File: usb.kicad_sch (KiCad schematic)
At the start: 53 parts, among them Q1 PJE138K, U1 MPFS250T-FCVG484, U13 USB3315-CP-TR, U15 SN74LVC1G04_SOT, U22 PI3USB102GZLEX, U23 PI3USB102GZLEX, U28 USB2422-I/MJ, Y1 Oscillator_24MHz_ESC_2016MV

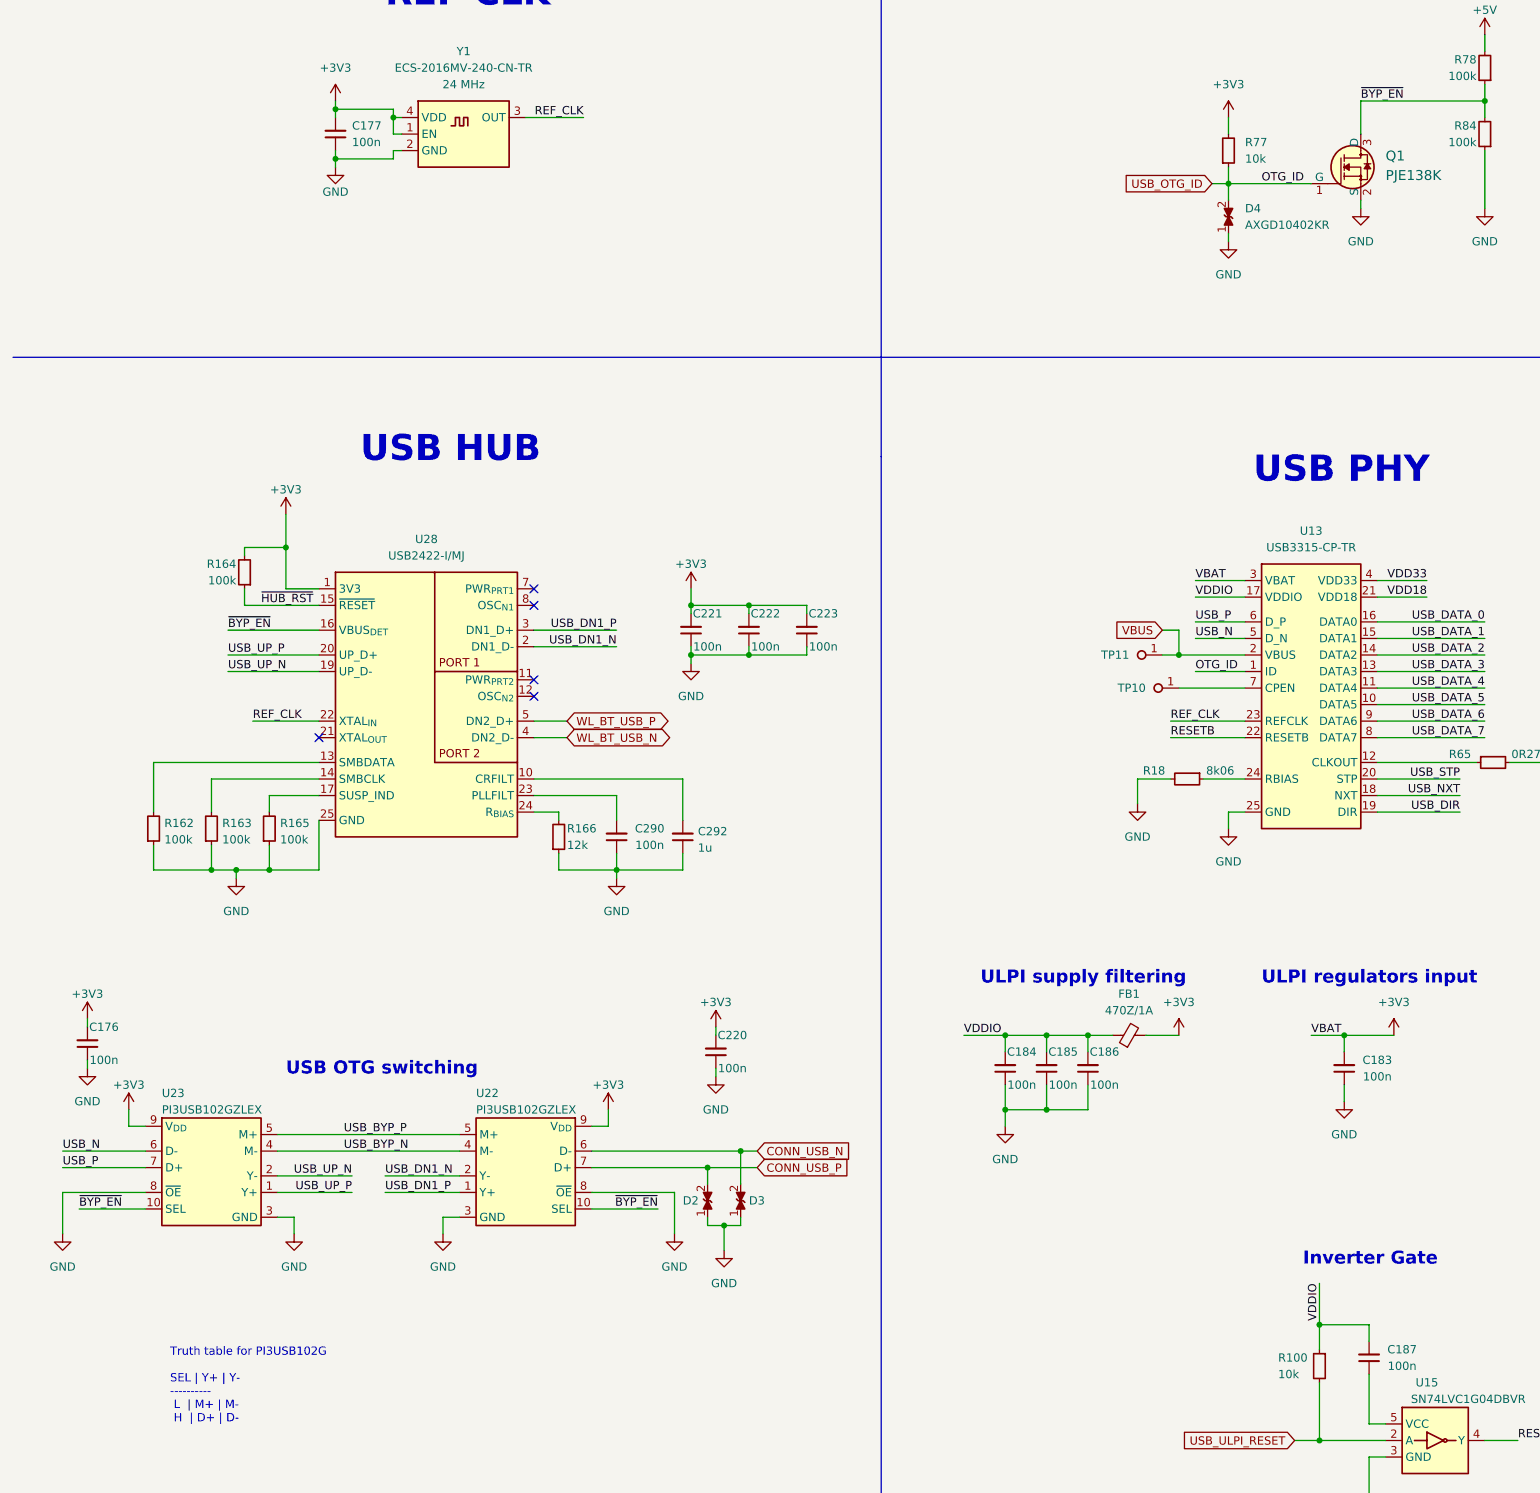
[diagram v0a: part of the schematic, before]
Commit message: [#56156] Create USB layout
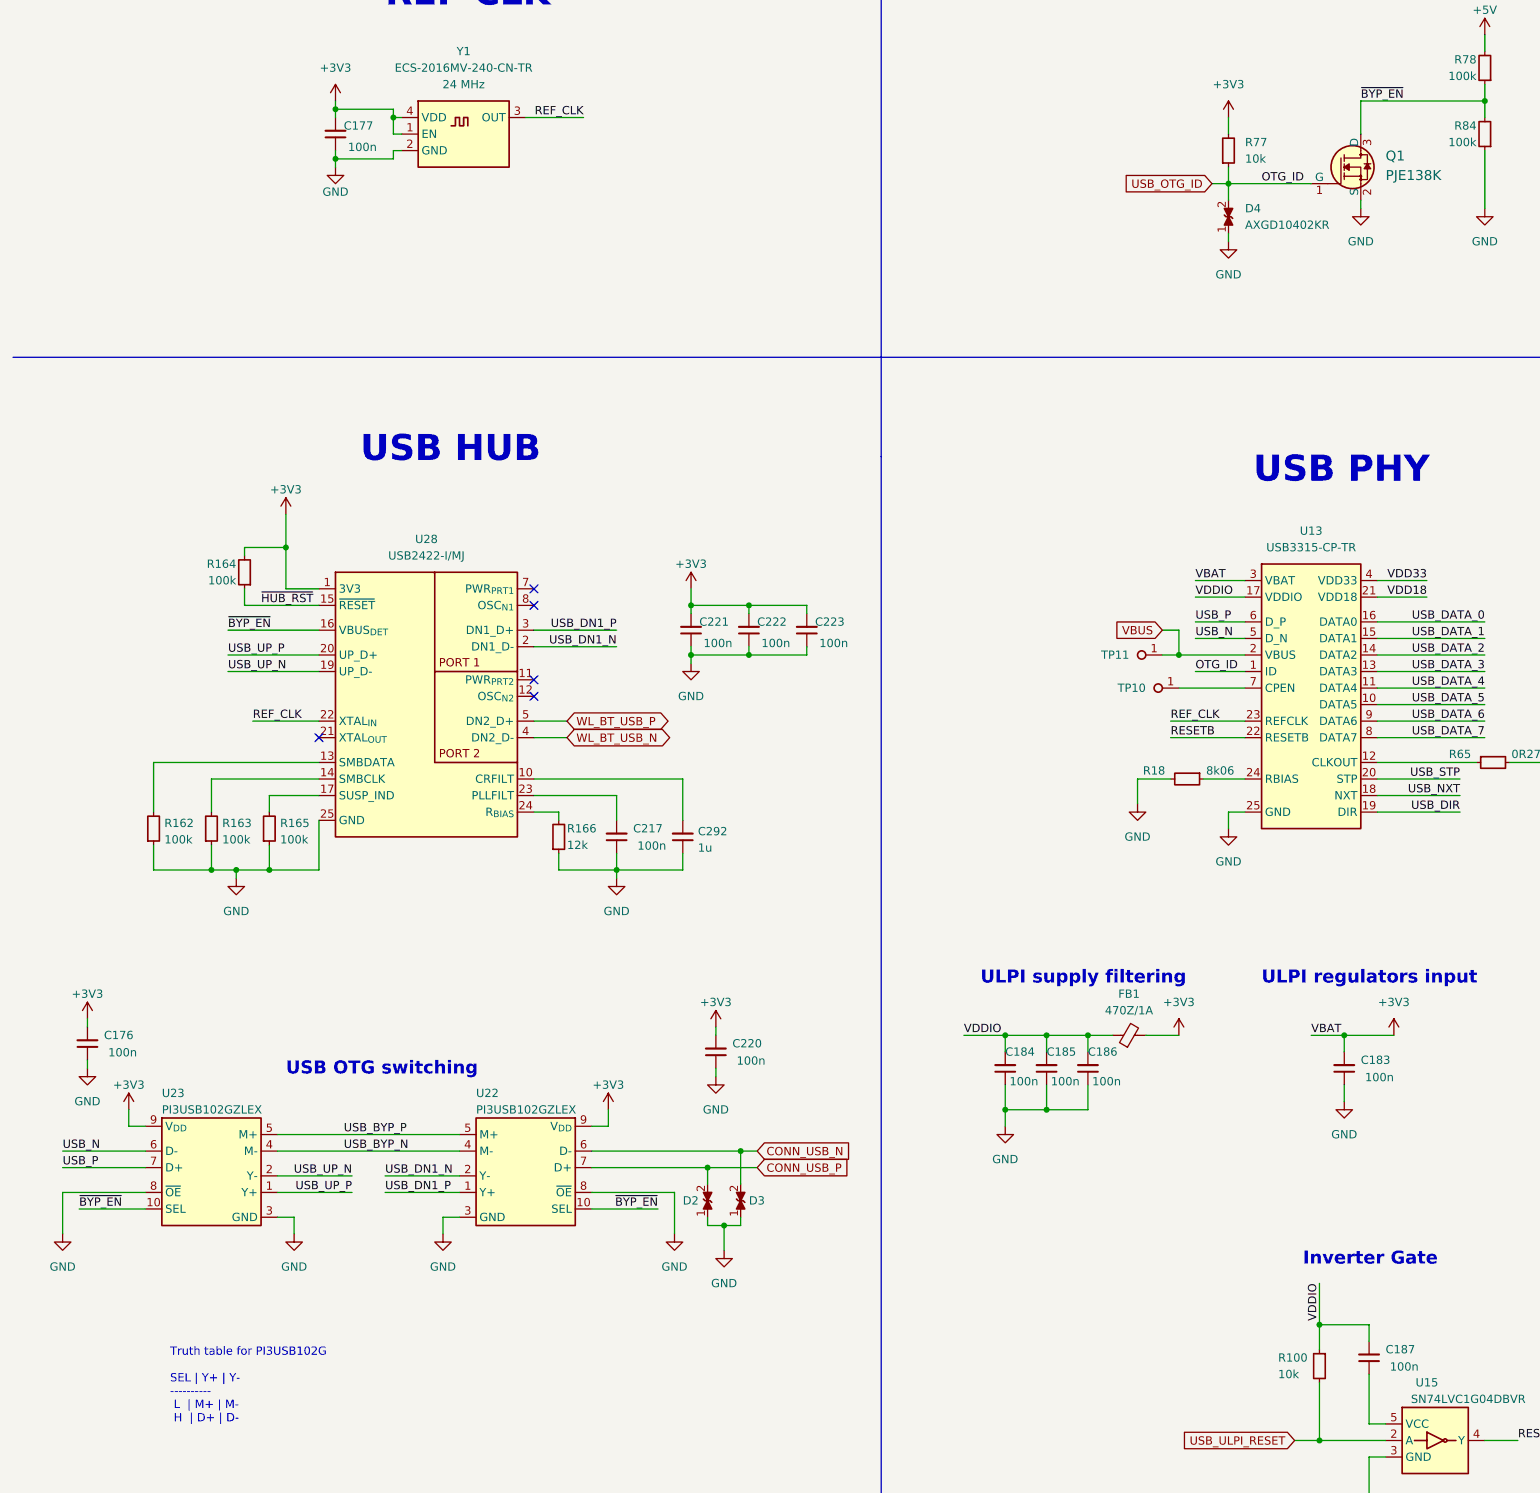
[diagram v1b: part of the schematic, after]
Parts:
- removed C176, C177, C183, C184, C185, C186, C187, C220, C221, C222, C223, C290: C_100n_0201_25V, antmicro-footprints:C_0201, symbol antmicroCapacitorsmisc:C_100n_0201_25V
- added C176, C177, C183, C184, C185, C186, C187, C217, C220, C221, C222, C223: C_100n_0402, antmicro-footprints:C_0402_1005Metric, symbol antmicroCapacitors0402:C_100n_0402
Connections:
- net +3V3: now also C176.2, C177.2, C183.2, C220.2, C221.2, C222.2, C223.2
- net GND: now also C176.1, C177.1, C183.1, C184.1, C185.1, C186.1, C217.1, C220.1, C221.1, C222.1, C223.1
- net VDDIO: now also C184.2, C185.2, C186.2, C187.2
- net at U15.5 (VCC): now also C187.1
- net at U28.23 (PLLFILT): now also C217.2

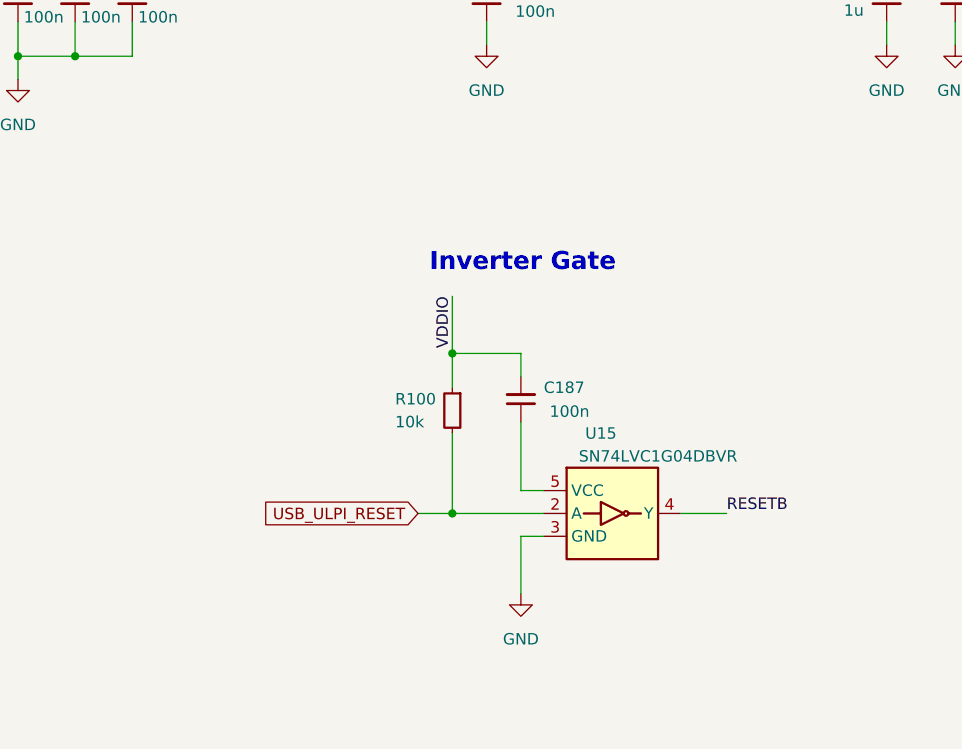
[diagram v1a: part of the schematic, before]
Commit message: [#56156] Add USB logic circuitry
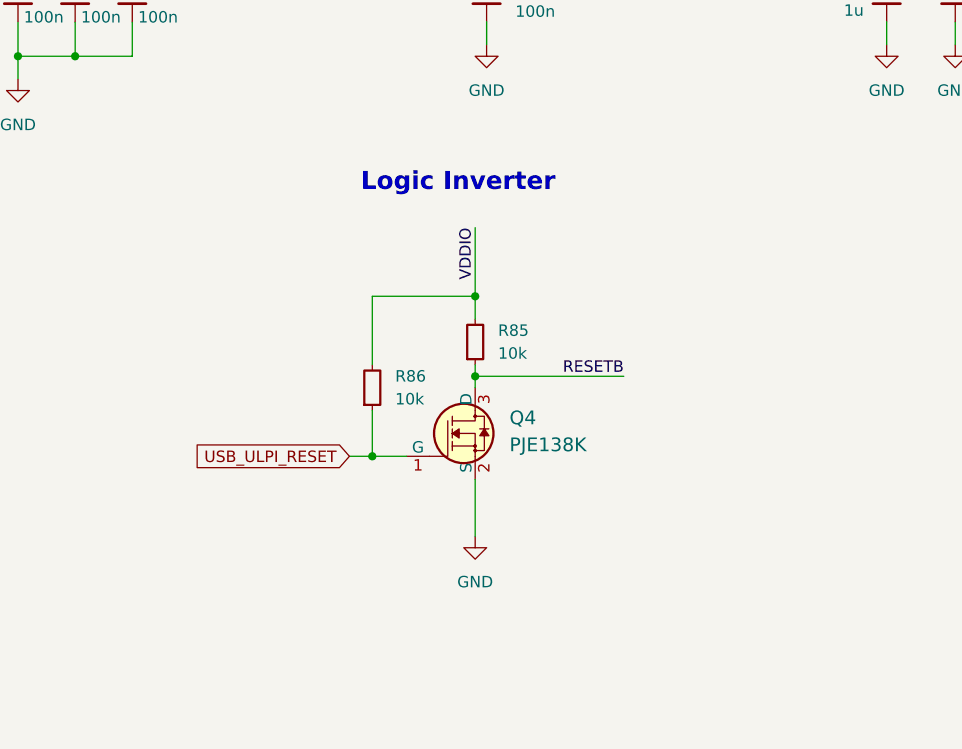
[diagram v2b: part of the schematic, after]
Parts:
- removed C187: C_100n_0402, antmicro-footprints:C_0402_1005Metric, symbol antmicroCapacitors0402:C_100n_0402
- removed R100: R_10k_0402, antmicro-footprints:R_0402_1005Metric, symbol antmicroResistors0402:R_10k_0402
- removed U15: SN74LVC1G04_SOT, antmicro-footprints:SOT-753, symbol antmicroLogicGatesandInverters:SN74LVC1G04_SOT
- added Q4: PJE138K, antmicro-footprints:SOT-523, symbol antmicroTransistorsFETsMOSFETsSingle:PJE138K
- added R85, R86: R_10k_0402, antmicro-footprints:R_0402_1005Metric, symbol antmicroResistors0402:R_10k_0402
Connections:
- net GND: now also Q4.2 (S)
- net RESETB: now also Q4.3 (D), R85.1
- net USB_ULPI_RESET: now also Q4.1 (G), R86.1
- net VDDIO: now also R85.2, R86.2
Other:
- note added: "Logic Inverter"
- note removed: "Inverter Gate"

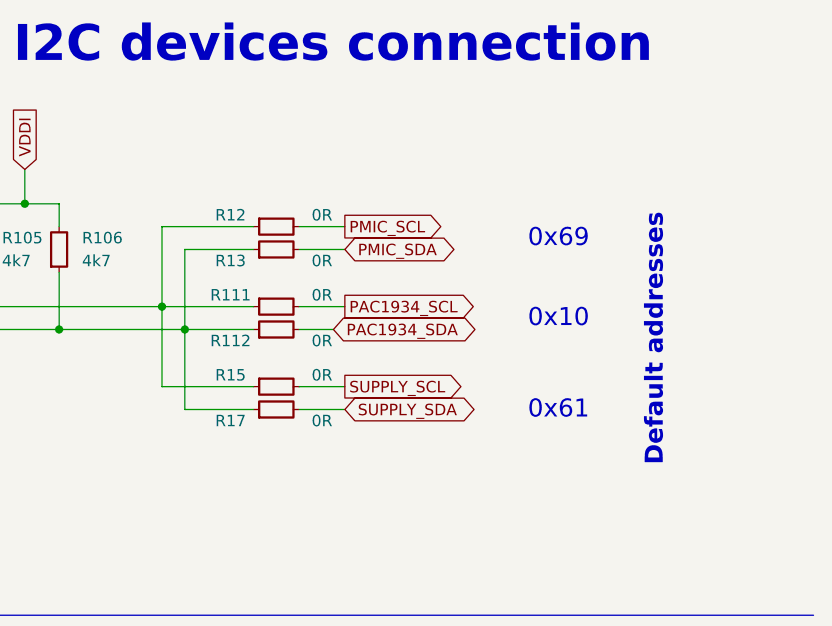
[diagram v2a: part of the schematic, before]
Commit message: [#56466] Remove I2C selector and JTAG chain
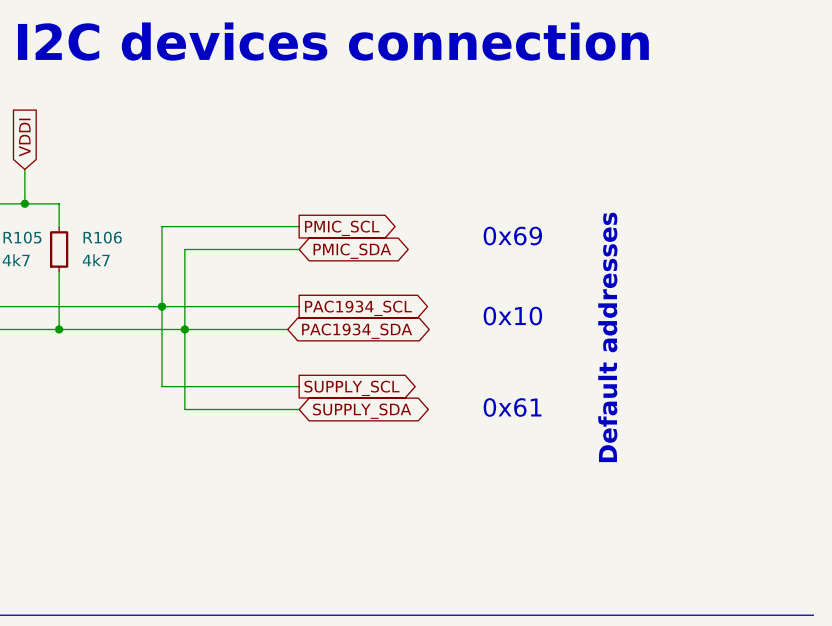
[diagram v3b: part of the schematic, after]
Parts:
- removed R111, R112, R12, R13, R15, R17: R_0R_0402, antmicro-footprints:R_0402_1005Metric, symbol antmicroResistors0402:R_0R_0402
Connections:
- net I2C_SCL is gone; now on net PAC1934_SCL: R105.1, U1.C1 (MSSIO26B2)
- net I2C_SDA is gone; now on net PAC1934_SDA: R106.1, U1.B1 (MSSIO27B2)
